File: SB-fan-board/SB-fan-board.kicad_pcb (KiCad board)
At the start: 2 copper layers, 51.6 x 35.1 mm, 17 parts, among them J1 FAN0, J2 FAN1, J3 NEO, J4 MAIN, U1 TPS54302

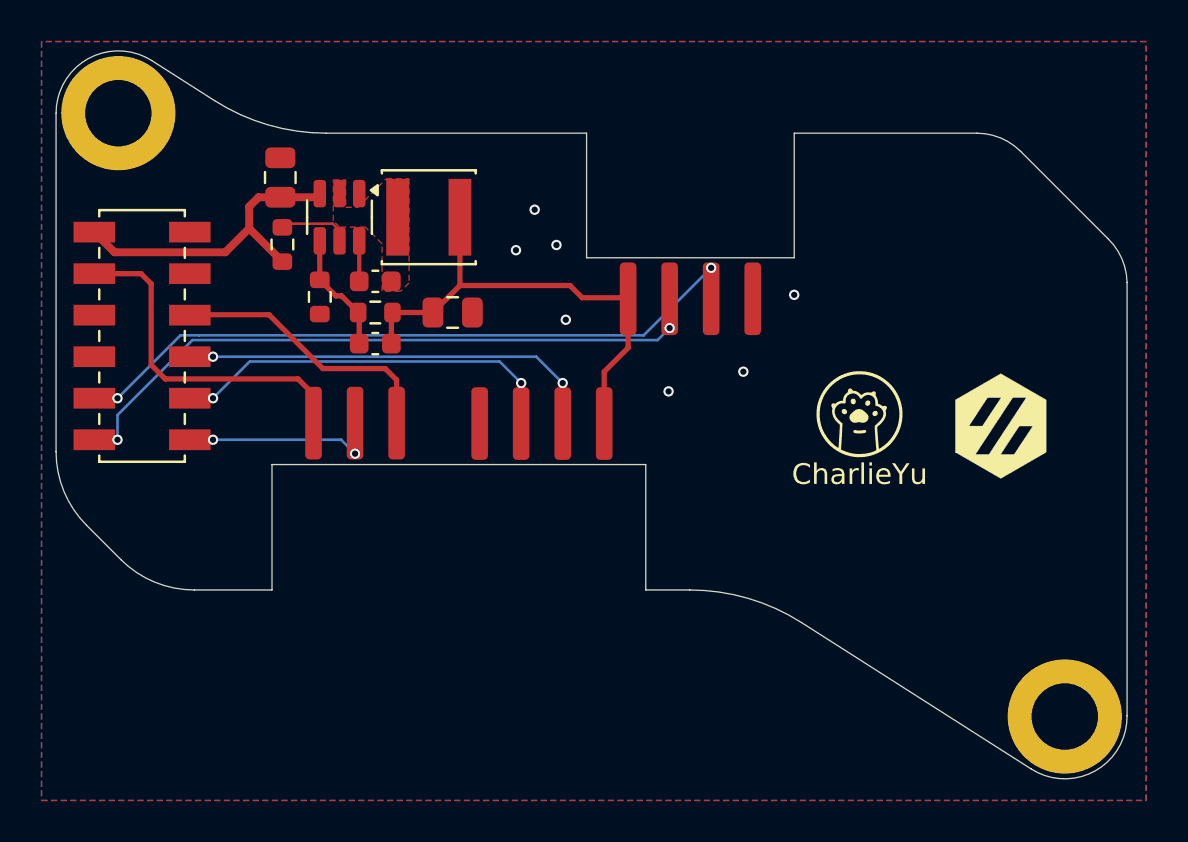
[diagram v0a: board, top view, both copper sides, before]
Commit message: update fan board to v2
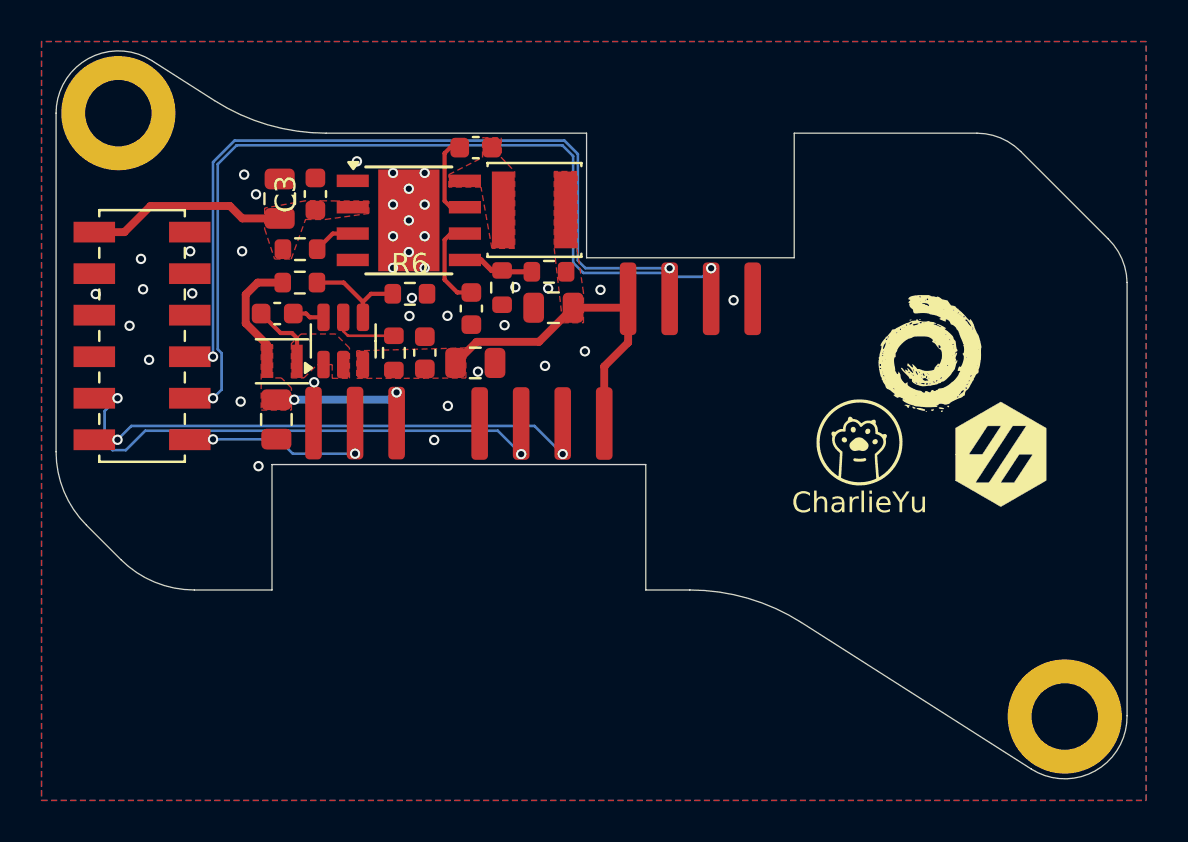
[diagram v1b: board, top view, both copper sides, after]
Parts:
- added C5: 1uF, Capacitor_SMD:C_0603_1608Metric, F.Cu at (162.2, 80.6)
- added C6: 100nF, Capacitor_SMD:C_0603_1608Metric, F.Cu at (152.8, 80.8)
- added C7: 10uF, Capacitor_SMD:C_0805_2012Metric, F.Cu at (162.4, 83.2)
- added C8: 100nF, Capacitor_SMD:C_0603_1608Metric, F.Cu at (160.0, 82.7)
- added C9: 22uF, Capacitor_SMD:C_0805_2012Metric, F.Cu at (152.8, 86.0)
- added L2: 2.2uH, Inductor_SMD:L_Murata_DFE201610P, F.Cu at (153.1, 83.2)
- added R4: 10K, Resistor_SMD:R_0603_1608Metric, F.Cu at (158.5, 82.7)
- added R5: 39K, Resistor_SMD:R_0603_1608Metric, F.Cu at (153.9, 79.4)
- added R6: 10K, Resistor_SMD:R_0603_1608Metric, F.Cu at (159.2, 79.9)
- added REF**: LOGO, Logos:Progynova, F.Cu at (184.3, 82.7)
- added U2: TPS565208, Package_TO_SOT_SMD:SOT-23-6, F.Cu at (156.0, 82.2)
- C2: value 10uF -> 4.7uF
- C3: value 22uF -> 220nF; footprint Capacitor_SMD:C_0805_2012Metric -> Capacitor_SMD:C_0603_1608Metric
- C4: value 82pF -> 22uF; footprint Capacitor_SMD:C_0603_1608Metric -> Capacitor_SMD:C_0805_2012Metric
- R3: value 5.23K -> 9.09K
- U1: value TPS54302 -> LMR33610BDDAR; footprint Package_TO_SOT_SMD:SOT-23-6 -> Package_SO:Texas_HSOP-8-1EP_3.9x4.9mm_P1.27mm
- moved R3 8.79 mm to (163.7, 79.6)
- moved C4 8.75 mm to (166.2, 80.6), turned to 180 degrees
- moved C3 8.73 mm to (154.7, 75.1), turned to 90 degrees
- moved R2 8.59 mm to (165.9, 78.8)
- moved C1 8.06 mm to (162.4, 72.9)
- moved L1 5.10 mm to (165.2, 75.9)
- moved U1 3.34 mm to (159.2, 76.4), turned to 0 degrees
- moved REF** 1.36 mm to (187.7, 87.6)
- moved RFF** 1.36 mm to (180.9, 87.1)
- moved C2 1.02 mm to (153.0, 75.3)
- moved R1 0.88 mm to (153.9, 77.8), turned to 0 degrees
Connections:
- C1 pad 1: Net-(U1-VBST) -> Net-(U1-BOOT)
- C2 pad 2: PGND -> GND
- C3 pad 1: +12V -> +24V
- C3 pad 2: PGND -> GND
- C4 pad 1: Net-(U1-VFB) -> +12V
- C4 pad 2: +12V -> GND
- H1 pad 1: PGND -> GND
- H2 pad 1: PGND -> GND
- J1 pad 2: /FAN0_DET -> /FAN1_DET
- J1 pad 3: /FAN0_PWM -> /FAN1_PWM
- J1 pad 4: PGND -> GND
- J2 pad 2: /FAN1_DET -> /FAN0_DET
- J2 pad 3: /FAN1_PWM -> /FAN0_PWM
- J2 pad 4: PGND -> GND
- J4 pad 10: PGND -> GND
- J4 pad 12: PGND -> GND
- J4 pad 8: +3V3 -> unconnected-(J4-Pin_8-Pad8)
- R2 pad 1: Net-(U1-VFB) -> Net-(U1-FB)
- R3 pad 1: Net-(U1-VFB) -> Net-(U1-FB)
- R3 pad 2: PGND -> GND
- U1 pad 1: PGND -> GND
- U1 pad 2: Net-(U1-SW) -> +24V
- U1 pad 3: +24V -> Net-(U1-EN)
- U1 pad 4: Net-(U1-VFB) -> unconnected-(U1-PG-Pad4)
- U1 pad 5: Net-(U1-EN) -> Net-(U1-FB)
- U1 pad 6: Net-(U1-VBST) -> Net-(U1-VCC)
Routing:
- net /FAN1_PWM: track 19.1 -> 42.6 mm
- net /FAN1_DET: track 20.5 -> 38.5 mm
- net GND: track 15.3 -> 0.00 mm, vias 0 -> 38
- net /FAN0_DET: track 31.6 -> 23.4 mm
- net /FAN0_PWM: track 32.3 -> 24.6 mm
- net +12V: track 23.5 -> 15.9 mm
- net Net-(U1-VFB): track 5.90 -> 0.00 mm
- net +24V: track 15.3 -> 9.70 mm
- net Net-(U2-VFB): track 0.00 -> 4.94 mm
- net Net-(U1-VCC): track 0.00 -> 4.57 mm
- net Net-(U1-BOOT): track 0.00 -> 4.24 mm
- net Net-(U1-FB): track 0.00 -> 3.37 mm
- net Net-(U2-SW): track 0.00 -> 3.34 mm
- net Net-(U2-EN): track 0.00 -> 3.20 mm
- net Net-(U1-VBST): track 1.95 -> 0.00 mm
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- added copper zone on F.Cu, net +12V
- added copper zone on F.Cu, net +24V
- added copper zone on F.Cu, net +3V3
- added copper zone on B.Cu, net GND
- added copper zone on F.Cu, net GND
- added copper zone on F.Cu, net Net-(U2-SW)
- removed copper zone on B.Cu, net PGND
- removed copper zone on F.Cu, net PGND

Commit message: silkscreen: add silkscreen
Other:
- board text added: "FAN0"
- board text added: "FAN1"
- board text added: "NEO"
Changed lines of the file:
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@@
 		(layer "B.SilkS")
+	)
+	(gr_poly
+		(pts
+			(xy 157.854001 87.346) (xy 157.6 87.6) (xy 157.345999 87.346)
+		)
+		(stroke
+			(width 0.15)
+			(type solid)
+		)
+		(fill solid)
+		(layer "F.SilkS")
+	)
+	(gr_poly
+		(pts
+			(xy 165.854001 87.3664) (xy 165.6 87.6204) (xy 165.345999 87.3664)
+		)
+		(stroke
+			(width 0.15)
+			(type solid)
+		)
+		(fill solid)
+		(layer "F.SilkS")
+	)
+	(gr_poly
+		(pts
+			(xy 172.495999 78.920327) (xy 172.75 78.666327) (xy 173.004001 78.920327)
+		)
+		(stroke
+			(width 0.15)
+			(type solid)
+		)
+		(fill solid)
+		(layer "F.SilkS")
 	)
 	(gr_circle
@@
 		)
 		(layer "Edge.Cuts")
+	)
+	(gr_text "NEO"
+		(at 157.6 87.219 270)
+		(layer "F.SilkS")
+		(effects
+			(font
+				(size 0.6 0.6)
+				(thickness 0.1)
+				(bold yes)
+			)
+			(justify right)
+		)
+	)
+	(gr_text "FAN1"
+		(at 172.75 79.047327 -90)
+		(layer "F.SilkS")
+		(effects
+			(font
+				(size 0.6 0.6)
+				(thickness 0.1)
+				(bold yes)
+			)
+			(justify left)
+		)
+	)
+	(gr_text "FAN0"
+		(at 165.6 87.2394 270)
+		(layer "F.SilkS")
+		(effects
+			(font
+				(size 0.6 0.6)
+				(thickness 0.1)
+				(bold yes)
+			)
+			(justify right)
+		)
 	)
 	(segment
@@
 		)
 	)
+	(group ""
+		(members "12d02d1b-7988-4606-8227-c5eb42250436" "ce3fdbe6-1bc9-4b35-a3d3-049165ca0a98")
+	)
+	(group ""
+		(members "cff4d07a-fa60-4dc1-b42f-63de56e8142c" "f17b4aa4-abb6-45d3-8595-9e014fe93101")
+	)
+	(group ""
+		(members "1d936151-aaa9-4463-b6c2-d9e88e780cd0" "e4f986cf-b90d-4d52-98c0-5aca04f34675")
+	)
 )
